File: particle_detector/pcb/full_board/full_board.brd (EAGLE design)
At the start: 64 x 32 mm, 43 parts, among them IC1 LT1807R, IC2 TLV3501, IC3 LT3461, IC4 TEENSY 3.2, IC5 SENSL-SIPM

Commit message: final routing for elecrow production, sent 2020.02.21
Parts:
- removed C10: 0.1uF, rcl:C0805
- removed C11: 2.2uF, rcl:C0805
- removed IC2: TLV3501, AU_Thinsat_Comparators:SOT23-6
- removed R11, R13: 47, resistor:M0805
- removed R12: 470, resistor:M0805
- removed TOUCH: (no value), pinhead:1X04
- added AMP, PEAK, RAW: (no value), pinhead:1X01
- moved IC5 81.9 mm to (16.0, 91.3), turned to 180 degrees
- moved R10 72.3 mm to (25.5, 74.0), flipped to the top, turned to 180 degrees
- moved C9 69.2 mm to (24.4, 71.0), flipped to the top
- moved R9 69.2 mm to (26.4, 71.0), flipped to the top
- moved D2 62.4 mm to (29.6, 68.0), flipped to the top
- moved R5 58.5 mm to (18.0, 71.0), flipped to the top, turned to 0 degrees
- moved XBUS2 57.4 mm to (28.6, 59.4), turned to 270 degrees
- moved R4 57.3 mm to (15.0, 70.0), flipped to the top
- moved C5 56.0 mm to (18.0, 69.0), flipped to the top, turned to 0 degrees
- moved C7 55.1 mm to (26.4, 67.0), flipped to the top, turned to 270 degrees
- moved C6 55.0 mm to (24.4, 67.0), flipped to the top, turned to 270 degrees
- moved C8 55.0 mm to (22.0, 64.0), flipped to the top
- moved R6 53.6 mm to (18.0, 73.0), flipped to the top, turned to 0 degrees
- moved R8 52.9 mm to (18.0, 65.0), flipped to the top, turned to 90 degrees
- moved R16 52.6 mm to (14.0, 73.0), flipped to the top, turned to 180 degrees
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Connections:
- removed net N$5: IC2.P$1, R11.2, R12.2
- removed net SIG_INT: IC2.P$5, IC4.17/A3, R13.2, TOUCH.4
- net 3.3V: no longer C10.1, C11.1, IC2.P$4, R12.1
- net AGND: no longer IC2.P$2, IC2.P$6, R11.1
- net GND: no longer C10.2, C11.2, R13.1
- net SIG_AMP: now also AMP.1; no longer IC2.P$3, TOUCH.2
- net SIG_PEAK: now also PEAK.1; no longer TOUCH.3
- net SIG_RAW: now also RAW.1; no longer TOUCH.1
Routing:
- net TX: track 0.46 -> 43.4 mm, vias 0 -> 2
- net AGND: track 0.00 -> 41.1 mm, vias 0 -> 3
- net 3.3V: track 0.00 -> 39.5 mm, vias 0 -> 4
- net SIG_AMP: track 0.00 -> 37.3 mm, vias 0 -> 1
- net SDA: track 0.60 -> 37.5 mm, vias 0 -> 1
- net RX: track 0.00 -> 36.6 mm
- net SCL: track 0.00 -> 35.8 mm, vias 0 -> 3
- net 5V: track 0.00 -> 29.9 mm, vias 0 -> 1
- net N$6: track 0.00 -> 27.5 mm
- net SIGNAL: track 0.00 -> 26.1 mm
- net SIG_RAW: track 0.00 -> 24.0 mm, vias 0 -> 1
- net N$2: track 0.00 -> 23.3 mm
- net SIG_PEAK: track 0.00 -> 18.9 mm
- net N$4: track 0.00 -> 17.0 mm
- net N$8: track 0.00 -> 15.3 mm
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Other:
- board size 64 x 32 mm -> 32 x 64 mm
- board text added: "American University ThinSat Team Created 2018-2020"
- board text added: "Particle Detector"
- board text removed: "AMP"
- board text removed: "INT"
- board text removed: "PEAK"
- board text removed: "RAW"

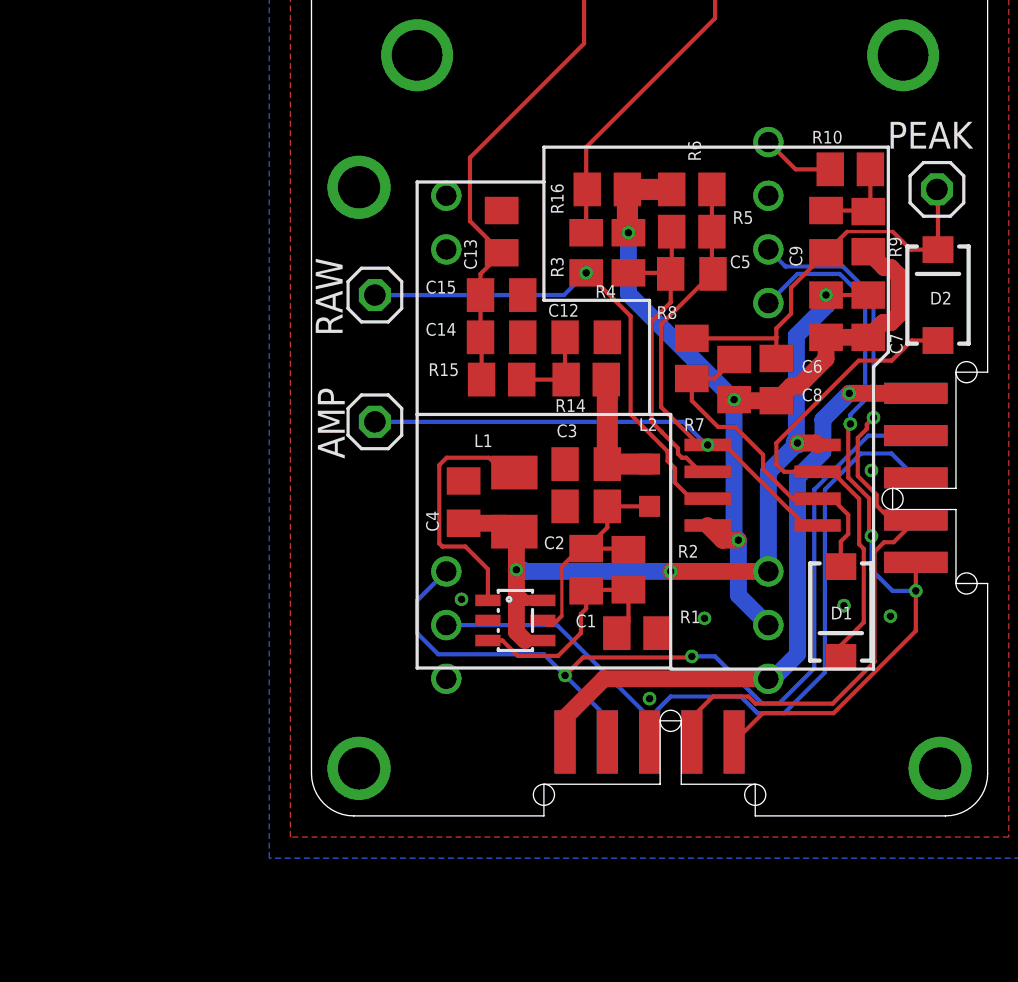
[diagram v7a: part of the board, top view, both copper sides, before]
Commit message: Swap the Teensy3.2 for the ATTiny and update nets.
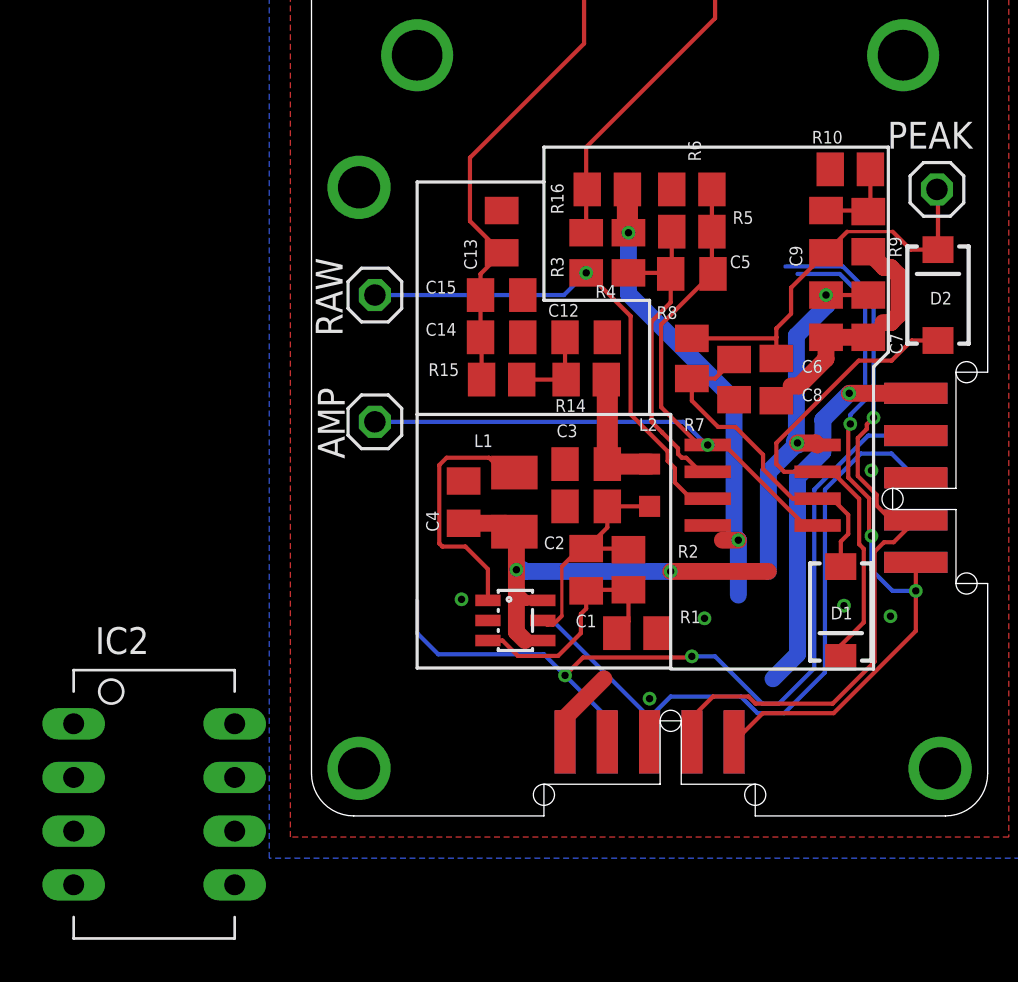
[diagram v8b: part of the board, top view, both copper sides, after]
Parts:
- removed IC4: TEENSY 3.2, personal:TEENSY_3.2_THINSAT
- added IC2: ATTINY5, personal:PDIP8
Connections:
- removed net 3.3V: C4.1, C6.1, C7.1, IC1.8, IC3.4, IC3.6, IC4.3.3V, L1.1
- removed net AGND: C6.2, C7.2, C8.2, IC1.4, IC4.AGND, R16.1, R4.1, R6.1, R7.1, R9.1
- net 5V: now also C4.1, C6.1, C7.1, IC1.8, IC2.P8, IC3.4, IC3.6, L1.1; no longer IC4.VIN
- net GND: now also C6.2, C7.2, C8.2, IC1.4, IC2.P4, R16.1, R4.1, R6.1, R7.1, R9.1; no longer IC4.GND
- net N$10: now also IC2.P6; no longer IC4.16/A2
- net RX: now also IC2.P2; no longer IC4.0
- net SCL: now also IC2.P7; no longer IC4.19/A5
- net SDA: now also IC2.P5; no longer IC4.18/A4
- net TX: now also IC2.P3; no longer IC4.1
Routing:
- net AGND: track 41.1 -> 0.00 mm, vias 3 -> 0
- net 3.3V: track 39.5 -> 0.00 mm, vias 4 -> 0
- net GND: track 0.00 -> 32.0 mm, vias 13 -> 15
- net 5V: track 29.9 -> 61.4 mm, vias 1 -> 5
- net RX: track 36.6 -> 31.3 mm
- net N$10: track 3.46 -> 0.00 mm
- net TX: track 43.4 -> 41.5 mm
- net SCL: track 35.8 -> 33.8 mm
- net SDA: track 37.5 -> 36.4 mm
